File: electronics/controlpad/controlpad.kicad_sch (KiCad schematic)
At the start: 6 parts, among them J1 USB - Host, SW1 START, U1 ESP32-C3 Mini, U2 MCP23017_SO

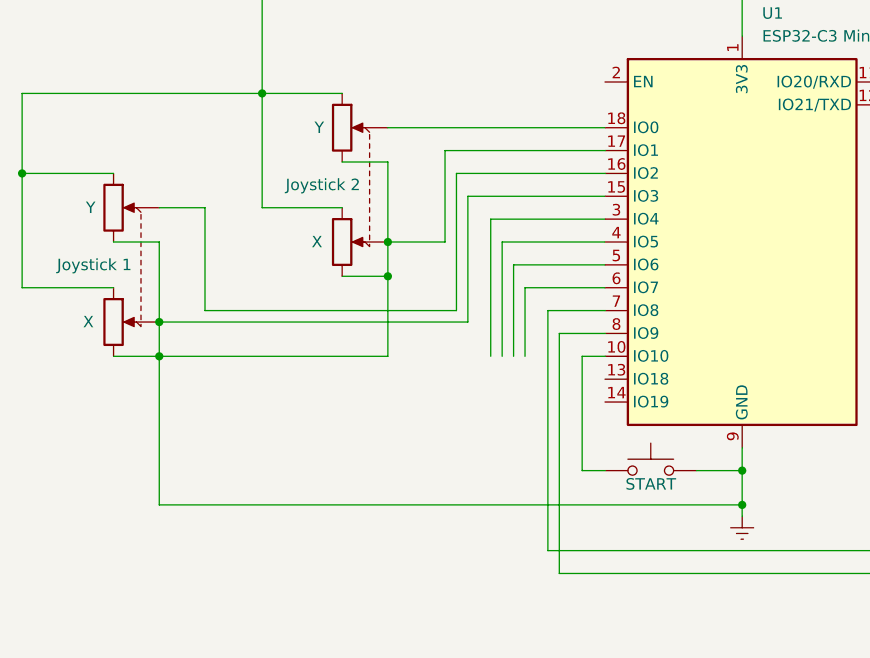
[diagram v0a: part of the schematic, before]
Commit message: Adding I/O to I2C expander, clearing few short circuits on joysticks
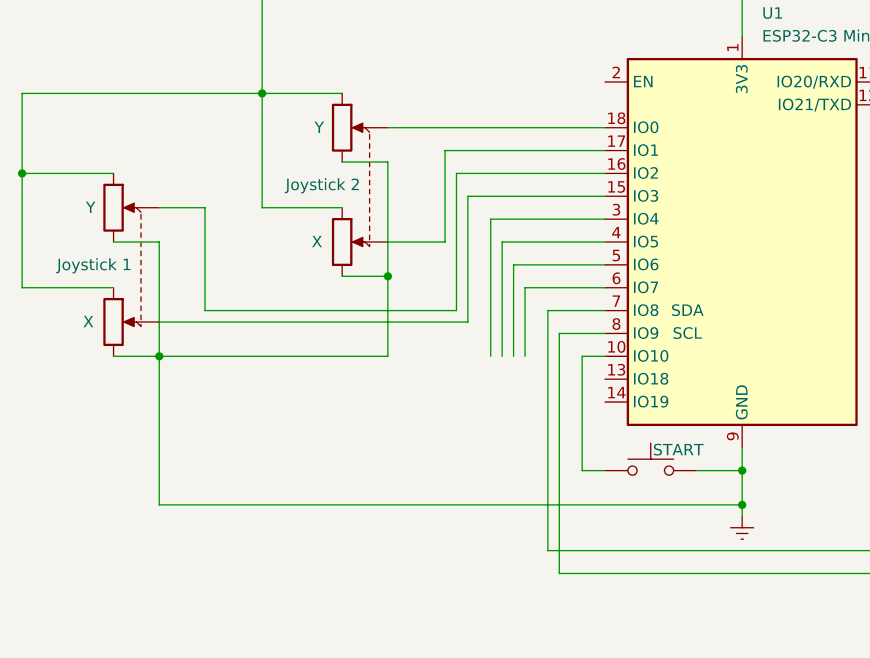
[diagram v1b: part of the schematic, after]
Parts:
- U1: Field5 (none) -> SDA; Field6 (none) -> SCL
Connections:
- net GNDREF: no longer RV1.5, RV2.5, U1.15 (IO3), U1.17 (IO1)
- new net: RV2.5, U1.15 (IO3)
- new net: RV1.5, U1.17 (IO1)
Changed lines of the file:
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@@
-	)
-	(junction
-		(at 39.37 76.2)
-		(diameter 0)
-		(color 0 0 0 0)
 	)
 	(junction
@@
 	)
 	(junction
-		(at 64.77 67.31)
-		(diameter 0)
-		(color 0 0 0 0)
-	)
-	(junction
 		(at 64.77 71.12)
 		(diameter 0)
@@
 	(wire
 		(pts
-			(xy 39.37 67.31) (xy 39.37 76.2)
+			(xy 39.37 67.31) (xy 39.37 80.01)
 		)
 		(stroke
@@
 	(wire
 		(pts
-			(xy 39.37 76.2) (xy 39.37 80.01)
-		)
-		(stroke
-			(width 0)
-			(type default)
-			(color 0 0 0 1)
-		)
-	)
-	(wire
-		(pts
 			(xy 64.77 54.61) (xy 88.9 54.61)
 		)
@@
 	(wire
 		(pts
-			(xy 64.77 67.31) (xy 64.77 71.12)
+			(xy 64.77 58.42) (xy 64.77 71.12)
 		)
 		(stroke
@@
 			(width 0)
 			(type default)
-		)
-	)
-	(wire
-		(pts
-			(xy 64.77 58.42) (xy 64.77 67.31)
-		)
-		(stroke
-			(width 0)
-			(type default)
-			(color 0 0 0 1)
 		)
 	)
@@
 		(on_board yes)
 		(dnp no)
-		(fields_autoplaced yes)
 		(property "Reference" "U1"
 			(at 106.3341 41.91 0)
@@
 				)
 				(hide yes)
+			)
+		)
+		(property "Field5" "SDA"
+			(at 98.044 74.93 0)
+			(effects
+				(font
+					(size 1.27 1.27)
+				)
+			)
+		)
+		(property "Field6" "SCL"
+			(at 98.044 77.47 0)
+			(effects
+				(font
+					(size 1.27 1.27)
+				)
 			)
 		)
@@
 		)
 		(property "Value" "START"
-			(at 93.98 94.234 0)
-			(effects
-				(font
+			(at 97.028 90.424 0)
+			(effects
+				(font

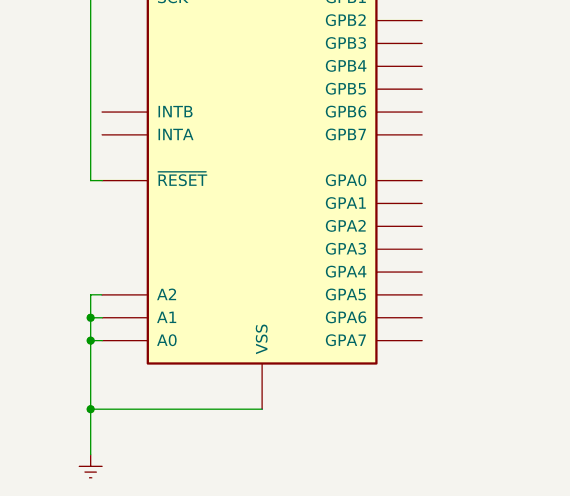
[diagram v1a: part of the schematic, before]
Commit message: Adding push buttons to GPA
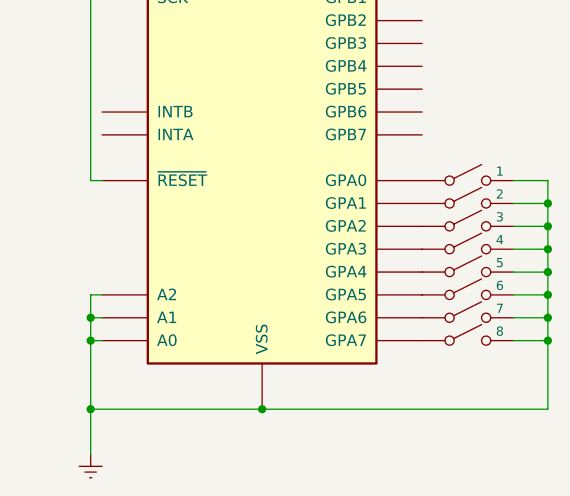
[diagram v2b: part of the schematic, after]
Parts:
- added SW10: 1, symbol Switch:SW_DPST_x2
- added SW2: 2, symbol Switch:SW_DPST_x2
- added SW3: 3, symbol Switch:SW_DPST_x2
- added SW4: 4, symbol Switch:SW_DPST_x2
- added SW5: 5, symbol Switch:SW_DPST_x2
- added SW6: 6, symbol Switch:SW_DPST_x2
- added SW7: 7, symbol Switch:SW_DPST_x2
- added SW8: 8, symbol Switch:SW_DPST_x2
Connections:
- net GNDREF: now also SW10.2 (B), SW2.2 (B), SW3.2 (B), SW4.2 (B), SW5.2 (B), SW6.2 (B), SW7.2 (B), SW8.2 (B)
- net at U2.21 (GPA0): now also SW10.1 (A)
- net at U2.22 (GPA1): now also SW2.1 (A)
- net at U2.23 (GPA2): now also SW3.1 (A)
- net at U2.24 (GPA3): now also SW4.1 (A)
- net at U2.25 (GPA4): now also SW5.1 (A)
- net at U2.26 (GPA5): now also SW6.1 (A)
- net at U2.27 (GPA6): now also SW7.1 (A)
- net at U2.28 (GPA7): now also SW8.1 (A)
